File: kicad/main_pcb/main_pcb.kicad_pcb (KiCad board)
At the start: 2 copper layers, 76 x 53.9 mm, 30 parts, among them J1 BAT_PWR, J2 LCD_I2C, J3 ECT_EXT, J4 EOT, J5 EOP, K2 3570.1331.051, Q1 PN2222A

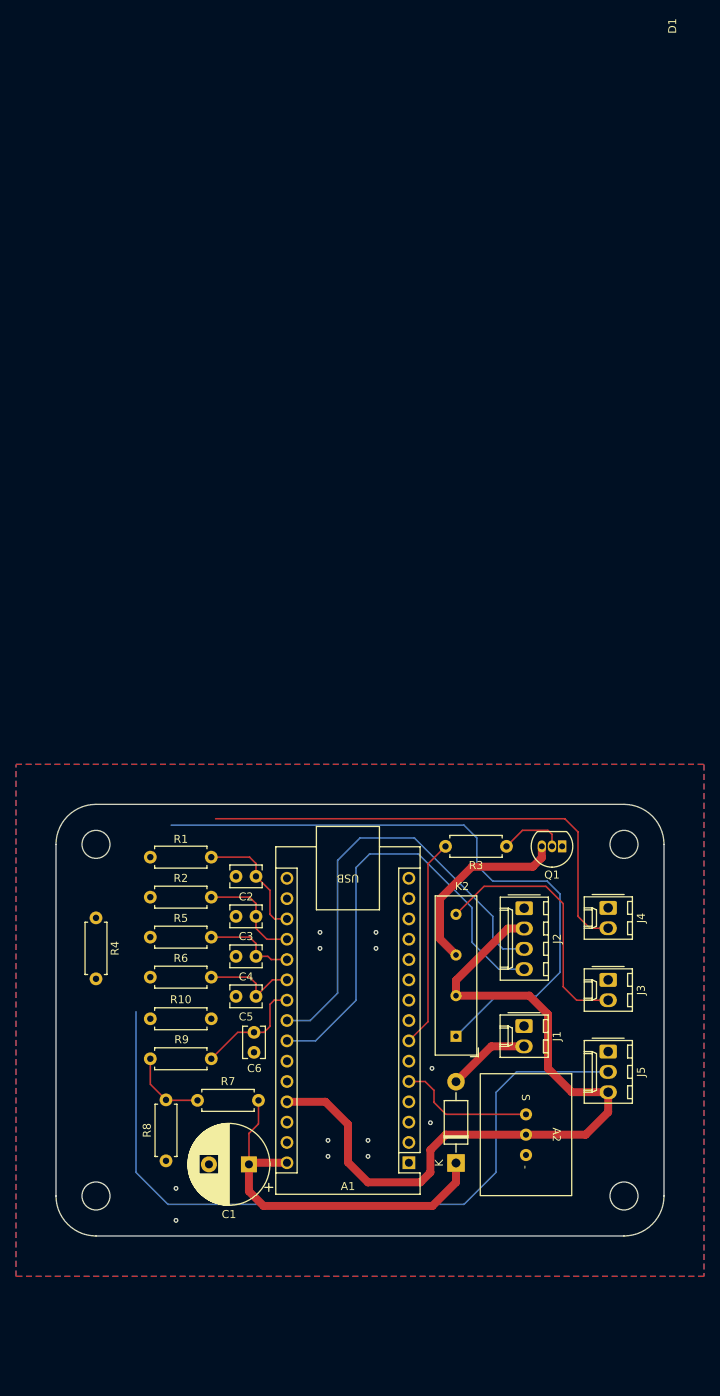
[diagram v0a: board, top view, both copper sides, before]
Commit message: Main PCB final design, refine eot calibration and limits
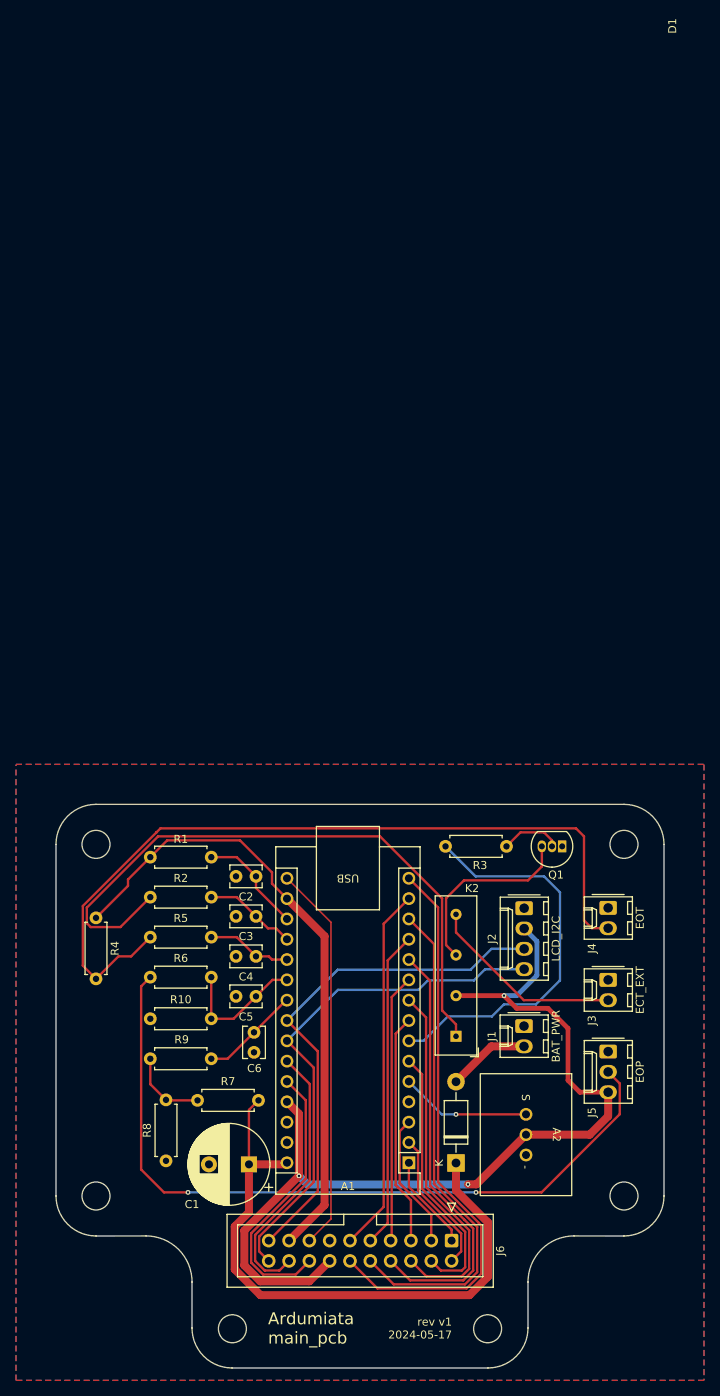
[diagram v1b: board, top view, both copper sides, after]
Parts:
- added H5: ~, MountingHole:MountingHole_3.5mm, F.Cu at (123.7, 140.2)
- added H6: ~, MountingHole:MountingHole_3.5mm, F.Cu at (155.6, 140.2)
- added J6: OUT_CON, Connector_IDC:IDC-Header_2x10_P2.54mm_Vertical, F.Cu at (151.1, 129.2)
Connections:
- A1 pad 1: unconnected-(A1-D1/TX-Pad1) -> OutTx
- A1 pad 10: unconnected-(A1-D7-Pad10) -> OutD7
- A1 pad 11: unconnected-(A1-D8-Pad11) -> OutD8
- A1 pad 12: unconnected-(A1-D9-Pad12) -> OutD9
- A1 pad 13: unconnected-(A1-D10-Pad13) -> OutD10
- A1 pad 14: unconnected-(A1-D11-Pad14) -> OutD11
- A1 pad 15: unconnected-(A1-D12-Pad15) -> OutD12
- A1 pad 16: unconnected-(A1-D13-Pad16) -> OutD13
- A1 pad 2: unconnected-(A1-D0/RX-Pad2) -> OutRx
- A1 pad 25: unconnected-(A1-A6-Pad25) -> OutA6
- A1 pad 26: unconnected-(A1-A7-Pad26) -> OutA7
- A1 pad 3: unconnected-(A1-~{RESET}-Pad3) -> OutReset
- A1 pad 6: unconnected-(A1-D3-Pad6) -> OutD3
- A1 pad 8: unconnected-(A1-D5-Pad8) -> OutD5
- A1 pad 9: unconnected-(A1-D6-Pad9) -> OutD6
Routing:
- net +3V3: track 0.00 -> 78.7 mm
- net OutD12: track 0.00 -> 71.8 mm
- net OutD10: track 0.00 -> 62.9 mm
- net OutD8: track 0.00 -> 54.0 mm
- net OutD13: track 0.00 -> 48.7 mm
- net OutD11: track 0.00 -> 45.8 mm
- net OutD6: track 0.00 -> 45.2 mm
- net OutD9: track 0.00 -> 39.7 mm
- net EOT_RAW: track 60.9 -> 99.7 mm
- net OutA7: track 0.00 -> 35.0 mm
- net OutA6: track 0.00 -> 34.2 mm
- net OutD3: track 0.00 -> 33.6 mm
- net OutD7: track 0.00 -> 33.5 mm
- net BAT_PWR: track 47.0 -> 77.0 mm
- net OutD5: track 0.00 -> 29.0 mm
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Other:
- board size 76 x 53.9 mm -> 76 x 70.4 mm
- board text added: "Ardumiata main_pcb"
- board text added: "rev v1 2024-05-17"

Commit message: Component adjustments and recalibration
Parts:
- R1: value 7k5 -> 6k8
- R7: value 33k -> 47k
- R8: value 5k -> 6k8
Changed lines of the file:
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@@
 			)
 		)
-		(property "Value" "5k"
+		(property "Value" "6k8"
 			(at 3.81 2.37 -90)
 			(layer "F.Fab")
@@
 			)
 		)
-		(property "Value" "7k5"
+		(property "Value" "6k8"
 			(at 3.81 2.37 180)
 			(layer "F.Fab")
@@
 			)
 		)
-		(property "Value" "33k"
+		(property "Value" "47k"
 			(at 3.81 2.37 0)
 			(layer "F.Fab")
